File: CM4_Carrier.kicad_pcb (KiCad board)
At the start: 4 copper layers, 160 x 90 mm, 87 parts, among them J1 Conn_01x03, J10 690-019-298-412, J11 USB_OTG, J12 10018783-11200TLF, J13 BM04B-GHS-TBT(LF)(SN)(N), J14 BM04B-GHS-TBT(LF)(SN)(N), J15 Conn_01x22_Female, J17 Molex 470531000, J18 BM04B-GHS-TBT(LF)(SN)(N), J19 XT30, J2 Conn_02x07_Odd_Even, J20 AMP171826-4, J21 BM04B-GHS-TBT(LF)(SN)(N), J3 Conn_01x03, J4 Conn_01x22_Female, J5 Conn_01x22_Female, J7 Micro_SD_Card_Det, Q1 DMP3013SFV-7, U1 TPD4EUSB30, U11 EMC2301-1-ACZL-TR, U12 RT9742SNGV, U13 FSUSB42MUX, U18 RT9742GGJ5, U2 TPD4EUSB30, U3 MagJack-A70-112-331N126, U4 TPD4EUSB30, U5 74LVC1G07SE-7, U6 USB2514B-I/M2, U7 AP22653W6, U9 74LVC1G07SE-7, Y1 24MHz

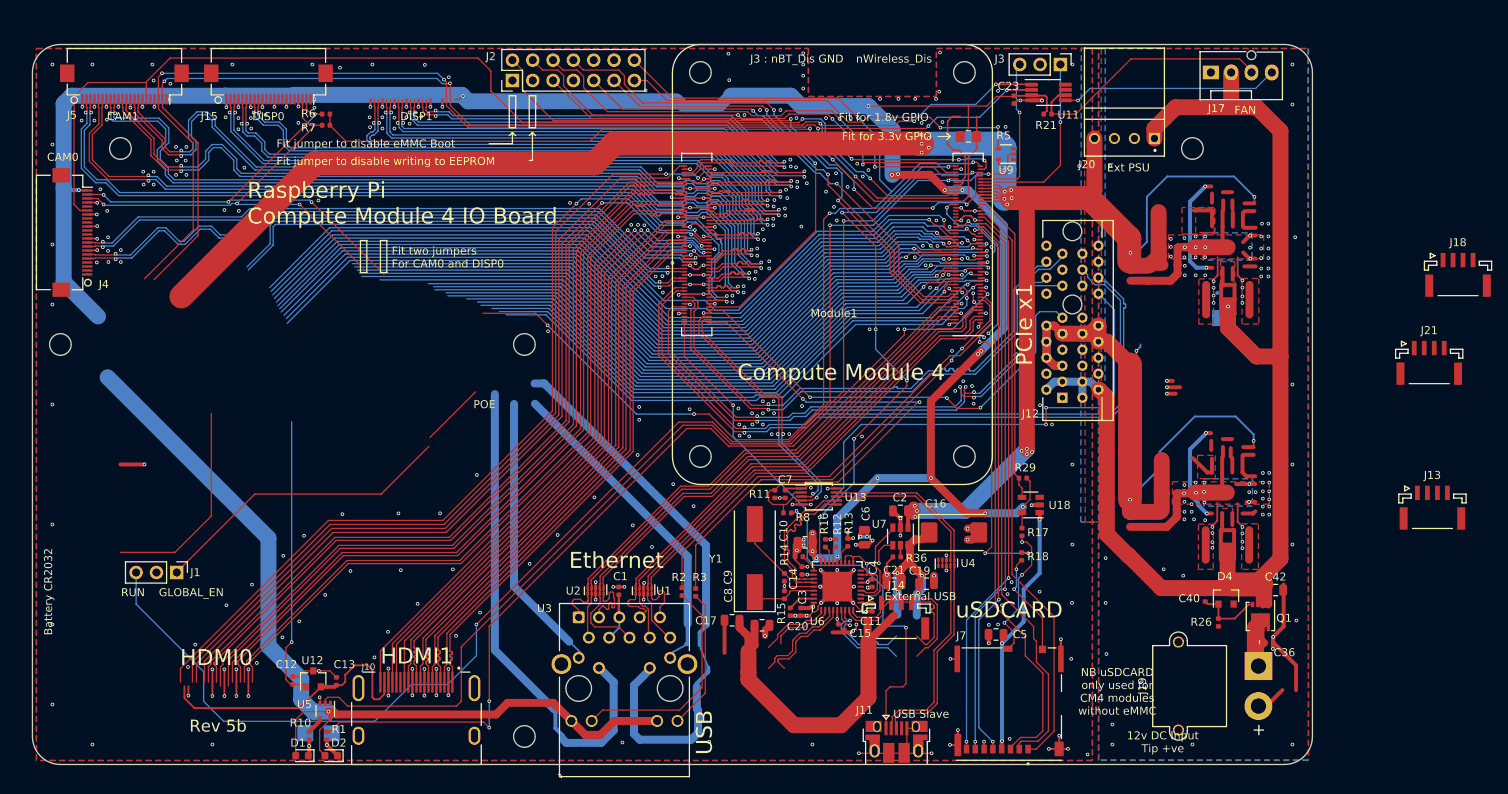
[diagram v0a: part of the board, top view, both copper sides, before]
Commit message: added original CM4IO pcb as starting point
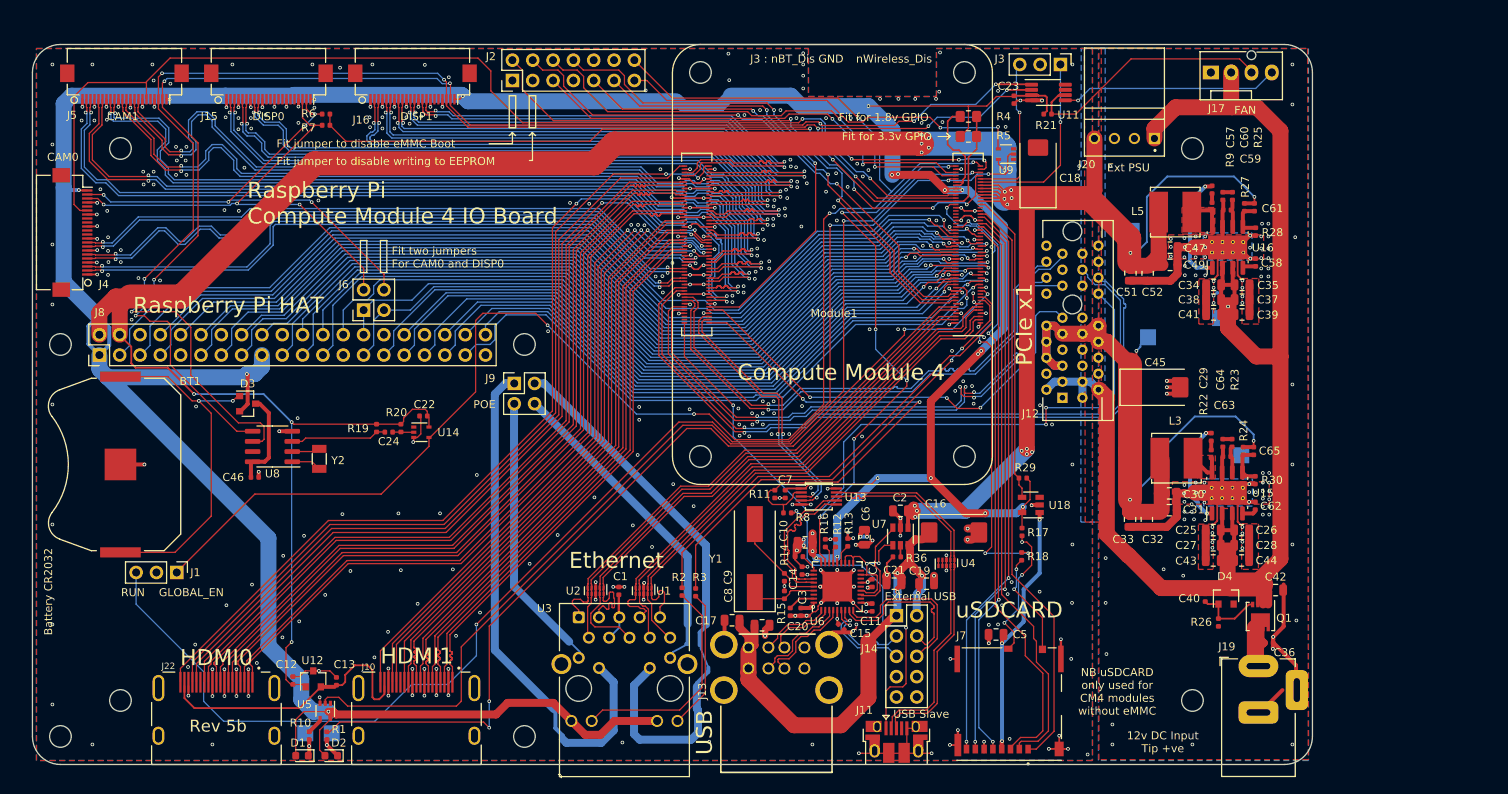
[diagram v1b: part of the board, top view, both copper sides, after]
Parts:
- removed J18, J21: BM04B-GHS-TBT(LF)(SN)(N), Connectors_JST:JST_GH_SM04B-GHS-TB_04x1.25mm_Angled
- added BT1: Battery_Cell, Battery:BatteryHolder_Keystone_3034_1x20mm, F.Cu at (90.0, 122.5)
- added C18: 100uF, Capacitor_Tantalum_SMD:CP_EIA-7343-31_Kemet-D, F.Cu at (204.7, 86.0)
- added C22: 100n, Capacitor_SMD:C_0402_1005Metric, F.Cu at (127.9, 116.4)
- added C24: 100n, Capacitor_SMD:C_0402_1005Metric, F.Cu at (123.5, 118.5)
- added C25: 10u 35v, Capacitor_SMD:C_0805_2012Metric, F.Cu at (226.6, 130.7)
- added C26: 10u 35v, Capacitor_SMD:C_0805_2012Metric, F.Cu at (230.2, 130.7)
- added C27: 10u 35v, Capacitor_SMD:C_0805_2012Metric, F.Cu at (226.6, 132.6)
- added C28: 10u 35v, Capacitor_SMD:C_0805_2012Metric, F.Cu at (230.2, 132.6)
- added C29: 100n, Capacitor_SMD:C_0402_1005Metric, F.Cu at (226.3, 119.1)
- added C30: 10u, Capacitor_SMD:C_0805_2012Metric, F.Cu at (221.1, 126.1)
- added C31: 10u, Capacitor_SMD:C_0805_2012Metric, F.Cu at (221.1, 128.2)
- added C32: 10u, Capacitor_SMD:C_0805_2012Metric, F.Cu at (218.3, 129.4)
- added C33: 10u, Capacitor_SMD:C_0805_2012Metric, F.Cu at (216.2, 129.4)
- added C34: 10u 35v, Capacitor_SMD:C_0805_2012Metric, F.Cu at (226.7, 100.0)
- added C35: 10u 35v, Capacitor_SMD:C_0805_2012Metric, F.Cu at (230.2, 100.0)
- added C37: 10u 35v, Capacitor_SMD:C_0805_2012Metric, F.Cu at (230.2, 101.9)
- added C38: 10u 35v, Capacitor_SMD:C_0805_2012Metric, F.Cu at (226.7, 101.9)
- added C39: 10u 35v, Capacitor_SMD:C_0805_2012Metric, F.Cu at (230.2, 103.8)
- added C41: 10u 35v, Capacitor_SMD:C_0805_2012Metric, F.Cu at (226.7, 103.8)
- added C43: 10u 35v, Capacitor_SMD:C_0805_2012Metric, F.Cu at (226.6, 134.5)
- added C44: 10u 35v, Capacitor_SMD:C_0805_2012Metric, F.Cu at (230.2, 134.5)
- added C45: 100uF, Capacitor_Tantalum_SMD:CP_EIA-7343-31_Kemet-D, F.Cu at (219.3, 112.8)
- added C46: 100n, Capacitor_SMD:C_0402_1005Metric, F.Cu at (106.8, 124.1)
- added C47: 10u, Capacitor_SMD:C_0805_2012Metric, F.Cu at (221.2, 95.4)
- added C49: 10u, Capacitor_SMD:C_0805_2012Metric, F.Cu at (221.2, 97.5)
- added C51: 10u, Capacitor_SMD:C_0805_2012Metric, F.Cu at (216.2, 98.6)
- added C52: 10u, Capacitor_SMD:C_0805_2012Metric, F.Cu at (218.4, 98.6)
- added C57: 100n, Capacitor_SMD:C_0402_1005Metric, F.Cu at (226.4, 88.2)
- added C58: 100n, Capacitor_SMD:C_0402_1005Metric, F.Cu at (231.9, 97.2)
- added C59: nf, Capacitor_SMD:C_0402_1005Metric, F.Cu at (228.3, 90.7)
- added C60: 1.2nF, Capacitor_SMD:C_0402_1005Metric, F.Cu at (227.8, 89.0)
- added C61: nf, Capacitor_SMD:C_0402_1005Metric, F.Cu at (231.8, 90.3)
- added C62: 100n, Capacitor_SMD:C_0402_1005Metric, F.Cu at (231.8, 127.7)
- added C63: nf, Capacitor_SMD:C_0402_1005Metric, F.Cu at (228.3, 121.5)
- added C64: 1.2nF, Capacitor_SMD:C_0402_1005Metric, F.Cu at (227.8, 119.8)
- added C65: nf, Capacitor_SMD:C_0402_1005Metric, F.Cu at (231.7, 120.8)
- added D3: BAT54C-7-F, Package_TO_SOT_SMD:SOT-23, F.Cu at (105.9, 114.9)
- added H1: MountingHole, MountingHole:MountingHole_2.7mm_M2.5, F.Cu at (90.0, 152.0)
- added H2: MountingHole, MountingHole:MountingHole_2.7mm_M2.5, F.Cu at (82.5, 156.5)
- added H8: MountingHole, MountingHole:MountingHole_2.7mm_M2.5, F.Cu at (224.0, 152.0)
- added J16: Conn_01x22_Female, CM4IO:Hirose_FH12-22S-0.5SH_1x22-1MP_P0.50mm_Horizontal, F.Cu at (126.5, 75.0)
- added J22: 690-019-298-412, CM4IO:EDAC 690-019-298-412, F.Cu at (102.0, 150.4)
- added J6: THD-02-R, Connector_PinHeader_2.54mm:PinHeader_2x02_P2.54mm_Vertical, F.Cu at (120.4, 103.2)
- added J8: THD-20-R, Connector_PinHeader_2.54mm:PinHeader_2x20_P2.54mm_Vertical, F.Cu at (87.4, 108.8)
- added J9: THD-02-R, Connector_PinHeader_2.54mm:PinHeader_2x02_P2.54mm_Vertical, F.Cu at (139.2, 112.4)
- added L3: SRN6045TA-3R3Y, Inductor_SMD:L_Bourns_SRN6045TA, F.Cu at (222.0, 121.7)
- added L5: SRN6045TA-3R3Y, Inductor_SMD:L_Bourns_SRN6045TA, F.Cu at (221.8, 91.0)
- added R19: 510K 1%, Resistor_SMD:R_0402_1005Metric, F.Cu at (122.0, 117.9)
- added R20: 510K 1%, Resistor_SMD:R_0402_1005Metric, F.Cu at (125.1, 117.9)
- added R22: 10R, Resistor_SMD:R_0402_1005Metric, F.Cu at (226.3, 121.2)
- added R23: 12K 1%, Resistor_SMD:R_0402_1005Metric, F.Cu at (228.9, 119.8)
- added R24: 47K 1%, Resistor_SMD:R_0402_1005Metric, F.Cu at (230.3, 120.8)
- added R25: 20K 1%, Resistor_SMD:R_0402_1005Metric, F.Cu at (229.0, 89.0)
- added R27: 12K 1%, Resistor_SMD:R_0402_1005Metric, F.Cu at (230.5, 90.3)
- added R28: 2.2K 1%, Resistor_SMD:R_0402_1005Metric, F.Cu at (231.9, 93.4)
- added R30: 15K 1%, Resistor_SMD:R_0402_1005Metric, F.Cu at (231.8, 124.5)
- added R4: nf, Resistor_SMD:R_0805_2012Metric_Pad1.15x1.40mm_HandSolder, F.Cu at (196.0, 79.0)
- added R9: 10R, Resistor_SMD:R_0402_1005Metric, F.Cu at (226.4, 90.2)
- added TP1: TestPoint, TestPoint:TestPoint_Pad_2.0x2.0mm, B.Cu at (218.4, 106.6)
- added TP4: TestPoint, TestPoint:TestPoint_Pad_2.0x2.0mm, B.Cu at (216.4, 93.3)
- added TP6: TestPoint, TestPoint:TestPoint_Pad_2.0x2.0mm, B.Cu at (230.1, 121.3)
- added U14: 74LVC1G07SE-7, Package_TO_SOT_SMD:SOT-353_SC-70-5, F.Cu at (127.6, 118.5)
- added U15: AP64501SP-13, CM4IO:SOIC-8-1EP_3.9x4.9mm_P1.27mm_EP2.95x4.9mm_Mask2.71x3.4mm_ThermalVias, F.Cu at (228.3, 126.1)
- added U16: AP64501SP-13, Package_SO:SOIC-8-1EP_3.9x4.9mm_P1.27mm_EP2.95x4.9mm_Mask2.71x3.4mm_ThermalVias, F.Cu at (228.4, 95.3)
- added U8: PCF85063AT/AAZ, Package_SO:SOIC-8_3.9x4.9mm_P1.27mm, F.Cu at (109.0, 120.2)
- added Y2: X32K768S301, Crystal:Crystal_SMD_3215-2Pin_3.2x1.5mm, F.Cu at (114.8, 121.8)
- J13: value BM04B-GHS-TBT(LF)(SN)(N) -> 690-008-221-904; footprint Connectors_JST:JST_GH_SM04B-GHS-TB_04x1.25mm_Angled -> CM4IO:MOLEX_USB_67298-4090
- J14: value BM04B-GHS-TBT(LF)(SN)(N) -> Conn_02x05_Odd_Even; footprint Connectors_JST:JST_GH_SM04B-GHS-TB_04x1.25mm_Angled -> Connector_PinHeader_2.54mm:PinHeader_2x05_P2.54mm_Vertical
- J19: value XT30 -> Barrel_Jack; footprint XT-30:AMASS_XT30PW-M_1x02_P2.50mm_Horizontal -> CM4IO:BarrelJack_Horizontal
- moved J13 85.2 mm to (172.0, 150.7)
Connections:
- C16 pad 1: /USB2-HUB/VBUS_HP -> /USB2-HUB/VBUS
- C17 pad 1: /USB2-HUB/VBUS_HP -> /USB2-HUB/VBUS
- C19 pad 1: /USB2-HUB/VBUS_HP -> /USB2-HUB/VBUS
- C20 pad 1: /USB2-HUB/VBUS_HP -> /USB2-HUB/VBUS
- C21 pad 1: /USB2-HUB/VBUS_HP -> /USB2-HUB/VBUS
- C40 pad 1: /PSUs/+12v -> /+12v
- C42 pad 1: /PSUs/+12v -> /+12v
- D4 pad 1: /PSUs/+12v -> /+12v
- J12 pad A2: /PCIe-connector/+12v -> /+12v
- J12 pad A3: /PCIe-connector/+12v -> /+12v
- J12 pad B1: /PCIe-connector/+12v -> /+12v
- J12 pad B2: /PCIe-connector/+12v -> /+12v
- J12 pad B3: /PCIe-connector/+12v -> /+12v
- J13 pad 1: /USB2-HUB/VBUS_HP -> /USB2-HUB/VBUS
- J13 pad 2: /USB2-HUB/HD2_N -> /USB2-HUB/HD1_N
- J13 pad 3: /USB2-HUB/HD2_P -> /USB2-HUB/HD1_P
- J14 pad 1: /USB2-HUB/VBUS_HP -> /USB2-HUB/VBUS
- J14 pad 2: /USB2-HUB/HD1_N -> /USB2-HUB/VBUS
- J14 pad 3: /USB2-HUB/HD1_P -> /USB2-HUB/HD3_N
- J14 pad 4: GND -> /USB2-HUB/HD4_N
- J17 pad 2: /+5v -> /+12v
- J19 pad 1: GND -> Net-(C36-Pad1)
- J19 pad 2: Net-(C36-Pad1) -> GND
- J20 pad 1: (no net) -> /+12v
- Module1 pad 51: /CM4_GPIO ( Ethernet, GPIO, SDCARD)/UART0_RX -> /CM4_GPIO ( Ethernet, GPIO, SDCARD)/GPIO15
- Module1 pad 55: /CM4_GPIO ( Ethernet, GPIO, SDCARD)/UART0_TX -> /CM4_GPIO ( Ethernet, GPIO, SDCARD)/GPIO14
- Q1 pad 1: /PSUs/+12v -> /+12v
- Q1 pad 2: /PSUs/+12v -> /+12v
- Q1 pad 3: /PSUs/+12v -> /+12v
- TP2 pad 1: /PSUs/+12v -> /+12v
- U11 pad 1: /FAN/SDA -> /SDA0
- U11 pad 2: /FAN/SCL -> /SCL0
- U6 pad 19: /USB2-HUB/nOCS2 -> /USB2-HUB/nOCS1
- U6 pad 21: /USB2-HUB/nOCS2 -> /USB2-HUB/nOCS1
- U7 pad 6: /USB2-HUB/VBUS_HP -> /USB2-HUB/VBUS
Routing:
- net GND: track 361.1 -> 882.7 mm, vias 477 -> 487
- net 12: track 189.7 -> 0.00 mm
- net /+12v: track 0.00 -> 189.7 mm, vias 0 -> 1
- net /CM4_GPIO ( Ethernet, GPIO, SDCARD)/GPIO14: track 0.00 -> 117.8 mm, vias 0 -> 1
- net /CM4_GPIO ( Ethernet, GPIO, SDCARD)/GPIO15: track 0.00 -> 114.7 mm, vias 0 -> 1
- net /CM4_GPIO ( Ethernet, GPIO, SDCARD)/UART0_TX: track 101.6 -> 0.00 mm, vias 1 -> 0
- net /CM4_GPIO ( Ethernet, GPIO, SDCARD)/UART0_RX: track 101.0 -> 0.00 mm, vias 1 -> 0
- net /USB2-HUB/VBUS: track 0.00 -> 69.2 mm, vias 0 -> 4
- net /+5v: track 301.3 -> 367.6 mm, vias 21 -> 23
- net /USB2-HUB/VBUS_HP: track 53.4 -> 0.00 mm, vias 4 -> 0
- net Net-(BT1-Pad1): track 0.00 -> 44.4 mm, vias 0 -> 2
- net 203: track 41.8 -> 0.00 mm
- net /+3.3v: track 419.7 -> 461.1 mm, vias 27 -> 28
- net /SCL0: track 167.3 -> 201.4 mm, vias 6 -> 8
- net /SDA0: track 165.6 -> 194.6 mm, vias 6 -> 8
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- added copper zone on F.Cu, net /+12v
- removed copper zone on F.Cu, net /PSUs/+12v
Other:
- board text added: "Raspberry Pi HAT"

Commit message: library management
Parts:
- removed BT1: Battery_Cell, Battery:BatteryHolder_Keystone_3034_1x20mm
- removed C32, C33, C47, C49, C51, C52: 10u, Capacitor_SMD:C_0805_2012Metric
- removed C34, C35, C37, C38, C39, C41, C43, C44: 10u 35v, Capacitor_SMD:C_0805_2012Metric
- removed C45: 100uF, Capacitor_Tantalum_SMD:CP_EIA-7343-31_Kemet-D
- removed C46, C57, C58, C62: 100n, Capacitor_SMD:C_0402_1005Metric
- removed C59, C61, C63, C65: nf, Capacitor_SMD:C_0402_1005Metric
- removed C60, C64: 1.2nF, Capacitor_SMD:C_0402_1005Metric
- removed D3: BAT54C-7-F, Package_TO_SOT_SMD:SOT-23
- removed J16: Conn_01x22_Female, CM4IO:Hirose_FH12-22S-0.5SH_1x22-1MP_P0.50mm_Horizontal
- removed J19: Barrel_Jack, CM4IO:BarrelJack_Horizontal
- removed J22: 690-019-298-412, CM4IO:EDAC 690-019-298-412
- removed L3, L5: SRN6045TA-3R3Y, Inductor_SMD:L_Bourns_SRN6045TA
- removed R20: 510K 1%, Resistor_SMD:R_0402_1005Metric
- removed R22: 10R, Resistor_SMD:R_0402_1005Metric
- removed R23, R27: 12K 1%, Resistor_SMD:R_0402_1005Metric
- removed R24: 47K 1%, Resistor_SMD:R_0402_1005Metric
- removed R25: 20K 1%, Resistor_SMD:R_0402_1005Metric
- removed R28: 2.2K 1%, Resistor_SMD:R_0402_1005Metric
- removed R30: 15K 1%, Resistor_SMD:R_0402_1005Metric
- removed TP1, TP2, TP4, TP6: TestPoint, TestPoint:TestPoint_Pad_2.0x2.0mm
- removed U14: 74LVC1G07SE-7, Package_TO_SOT_SMD:SOT-353_SC-70-5
- removed U15: AP64501SP-13, CM4IO:SOIC-8-1EP_3.9x4.9mm_P1.27mm_EP2.95x4.9mm_Mask2.71x3.4mm_ThermalVias
- removed U16: AP64501SP-13, Package_SO:SOIC-8-1EP_3.9x4.9mm_P1.27mm_EP2.95x4.9mm_Mask2.71x3.4mm_ThermalVias
- removed Y2: X32K768S301, Crystal:Crystal_SMD_3215-2Pin_3.2x1.5mm
- added C48: 10u, Capacitor_SMD:C_0805_2012Metric, F.Cu at (119.6, 101.0)
- added C50: 100uF, Capacitor_Tantalum_SMD:CP_EIA-7343-31_Kemet-D, F.Cu at (108.0, 102.4)
- added C53: 10u, Capacitor_SMD:C_0805_2012Metric, F.Cu at (115.2, 101.0)
- added C54: 10u, Capacitor_SMD:C_0805_2012Metric, F.Cu at (125.8, 90.2)
- added C55: 10u, Capacitor_SMD:C_0805_2012Metric, F.Cu at (115.2, 104.0)
- added C56: 10u, Capacitor_SMD:C_0805_2012Metric, F.Cu at (125.8, 93.2)
- added J18: BM04B-GHS-TBT(LF)(SN)(N), Connectors_JST:JST_GH_SM04B-GHS-TB_04x1.25mm_Angled, F.Cu at (151.2, 38.4)
- added J21: BM04B-GHS-TBT(LF)(SN)(N), Connectors_JST:JST_GH_SM04B-GHS-TB_04x1.25mm_Angled, F.Cu at (160.4, 38.4)
- added L1: 4.7uH, Open-HD:IND_XAL6060-472MEB, F.Cu at (139.4, 94.7)
- added R31: 49.9k, Resistor_SMD:R_0402_1005Metric, F.Cu at (130.2, 85.2)
- added U10: AP22653W6, Package_TO_SOT_SMD:SOT-23-6, F.Cu at (126.1, 86.4)
- C18: value 100uF -> 10uF; footprint Capacitor_Tantalum_SMD:CP_EIA-7343-31_Kemet-D -> Capacitor_SMD:C_1210_3225Metric
- C22: value 100n -> 10uF; footprint Capacitor_SMD:C_0402_1005Metric -> Capacitor_SMD:C_1210_3225Metric
- C24: value 100n -> 220nF; footprint Capacitor_SMD:C_0402_1005Metric -> Capacitor_SMD:C_0603_1608Metric
- C25: value 10u 35v -> 1uF; footprint Capacitor_SMD:C_0805_2012Metric -> Capacitor_SMD:C_0402_1005Metric
- C26: value 10u 35v -> 100nF; footprint Capacitor_SMD:C_0805_2012Metric -> Capacitor_SMD:C_0402_1005Metric
- C27: value 10u 35v -> 10pF; footprint Capacitor_SMD:C_0805_2012Metric -> Capacitor_SMD:C_0402_1005Metric
- C28: value 10u 35v -> 22uF
- C29: value 100n -> 22uF; footprint Capacitor_SMD:C_0402_1005Metric -> Capacitor_SMD:C_0805_2012Metric
- C30: value 10u -> 22uF
- C31: value 10u -> 100nF; footprint Capacitor_SMD:C_0805_2012Metric -> Capacitor_SMD:C_0603_1608Metric
- J13: value 690-008-221-904 -> BM04B-GHS-TBT(LF)(SN)(N); footprint CM4IO:MOLEX_USB_67298-4090 -> Connectors_JST:JST_GH_SM04B-GHS-TB_04x1.25mm_Angled
- J14: value Conn_02x05_Odd_Even -> BM04B-GHS-TBT(LF)(SN)(N); footprint Connector_PinHeader_2.54mm:PinHeader_2x05_P2.54mm_Vertical -> Connectors_JST:JST_GH_SM04B-GHS-TB_04x1.25mm_Angled
- J15: footprint CM4IO:Hirose_FH12-22S-0.5SH_1x22-1MP_P0.50mm_Horizontal -> Connector_FFC-FPC:Hirose_FH12-22S-0.5SH_1x22-1MP_P0.50mm_Horizontal
- J4, J5: value Conn_01x22_Female -> DF40C-24DP-0.4V_51_; footprint CM4IO:Hirose_FH12-22S-0.5SH_1x22-1MP_P0.50mm_Horizontal -> Open-HD:DF40C24DP04V51
- J8: value THD-20-R -> HDMI_D_1.4; footprint Connector_PinHeader_2.54mm:PinHeader_2x20_P2.54mm_Vertical -> Connector_HDMI:HDMI_Micro-D_Molex_46765-0x01
- J9: value THD-02-R -> Conn_02x08_Odd_Even; footprint Connector_PinHeader_2.54mm:PinHeader_2x02_P2.54mm_Vertical -> Connector_PinHeader_2.54mm:PinHeader_2x08_P2.54mm_Vertical
- R19: value 510K 1% -> 24.9k
- R4: value nf -> 100k; footprint Resistor_SMD:R_0805_2012Metric_Pad1.15x1.40mm_HandSolder -> Resistor_SMD:R_0402_1005Metric
- R9: value 10R -> 100k
- U11: footprint Package_SO:MSOP-8_3x3mm_P0.65mm -> Package_SO:SOIC-8_5.23x5.23mm_P1.27mm
- U8: value PCF85063AT/AAZ -> LMR33640DDDAR; footprint Package_SO:SOIC-8_3.9x4.9mm_P1.27mm -> Open-HD:NOPB
- moved J13 119.0 mm to (132.7, 38.4), turned to 180 degrees
- moved C1 113.7 mm to (259.4, 176.7)
- moved R2 113.7 mm to (267.2, 176.8)
- moved U3 113.7 mm to (260.1, 188.9)
- moved R3 113.7 mm to (268.9, 176.9)
- moved U1 113.7 mm to (262.4, 176.7)
- moved U2 113.7 mm to (256.4, 176.7)
- moved J14 112.4 mm to (141.9, 38.4), turned to 180 degrees
- moved J4 98.5 mm to (173.4, 52.2), turned to 90 degrees
- moved J5 96.5 mm to (184.3, 52.3), turned to 90 degrees
- moved C10 94.0 mm to (148.8, 222.4)
- moved C14 94.0 mm to (148.4, 225.9)
- moved C16 94.0 mm to (167.4, 221.1)
- moved C17 94.0 mm to (139.7, 232.1)
- moved C19 94.0 mm to (164.0, 227.5)
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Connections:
- C16 pad 1: /USB2-HUB/VBUS -> /USB2-HUB/VBUS_HP
- C17 pad 1: /USB2-HUB/VBUS -> /USB2-HUB/VBUS_HP
- C18 pad 1: /+5v -> /PSUs/+12v
- C19 pad 1: /USB2-HUB/VBUS -> /USB2-HUB/VBUS_HP
- C20 pad 1: /USB2-HUB/VBUS -> /USB2-HUB/VBUS_HP
- C21 pad 1: /USB2-HUB/VBUS -> /USB2-HUB/VBUS_HP
- C22 pad 1: /+5v -> /PSUs/+12v
- C24 pad 1: Net-(C24-Pad1) -> /PSUs/+12v
- C24 pad 2: /RTC , Wakeup, FAN/nRTC_INT -> GND
- C25 pad 1: /+12v -> Net-(C25-Pad1)
- C26 pad 1: /+12v -> Net-(C26-Pad1)
- C26 pad 2: GND -> Net-(C26-Pad2)
- C27 pad 1: /+12v -> /+5v
- C27 pad 2: GND -> Net-(C27-Pad2)
- C28 pad 1: /+12v -> /+5v
- C29 pad 1: Net-(C29-Pad1) -> /+5v
- C29 pad 2: Net-(C29-Pad2) -> GND
- C30 pad 1: /PCIe-connector/+3.3v -> /+5v
- C31 pad 1: /PCIe-connector/+3.3v -> /+5v
- C40 pad 1: /+12v -> /PSUs/+12v
- C42 pad 1: /+12v -> /PSUs/+12v
- D4 pad 1: /+12v -> /PSUs/+12v
- J12 pad A2: /+12v -> Net-(J12-PadA2)
- J12 pad A3: /+12v -> Net-(J12-PadA2)
- J12 pad B1: /+12v -> Net-(J12-PadB1)
- J12 pad B2: /+12v -> Net-(J12-PadB1)
- J12 pad B3: /+12v -> Net-(J12-PadB1)
- J13 pad 1: /USB2-HUB/VBUS -> /USB2-HUB/VBUS_HP
- J13 pad 2: /USB2-HUB/HD1_N -> /USB2-HUB/HD2_N
- J13 pad 3: /USB2-HUB/HD1_P -> /USB2-HUB/HD2_P
- J14 pad 1: /USB2-HUB/VBUS -> /USB2-HUB/VBUS_HP
- J14 pad 2: /USB2-HUB/VBUS -> /USB2-HUB/HD1_N
- J14 pad 3: /USB2-HUB/HD3_N -> /USB2-HUB/HD1_P
- J14 pad 4: /USB2-HUB/HD4_N -> GND
- J17 pad 2: /+12v -> /+5v
- J4 pad 1: GND -> /CM4_HighSpeed/CAM1_D0_N
- J4 pad 10: GND -> Net-(J4-Pad10)
- J4 pad 11: Net-(J4-Pad11) -> GND
- J4 pad 13: GND -> /CM4_HighSpeed/CAM1_C_N
- J4 pad 14: Net-(J4-Pad14) -> /CAM_GPIO
- J4 pad 15: Net-(J4-Pad15) -> /CM4_HighSpeed/CAM1_C_P
- J4 pad 16: GND -> Net-(J4-Pad16)
- J4 pad 17: /CAM_GPIO -> GND
- J4 pad 18: Net-(J4-Pad18) -> GND
- J4 pad 19: GND -> /CM4_HighSpeed/CAM1_D2_N
- J4 pad 2: /CM4_HighSpeed/CAM0_D0_N -> /CM4_HighSpeed/CAM1_D3_N
- J4 pad 20: /CM4_HighSpeed/SCL1 -> /SCL0
- J4 pad 21: /CM4_HighSpeed/SDA1 -> /CM4_HighSpeed/CAM1_D2_P
- J4 pad 22: /+3.3v -> /SDA0
- J4 pad 3: /CM4_HighSpeed/CAM0_D0_P -> /CM4_HighSpeed/CAM1_D0_P
- J4 pad 4: GND -> /CM4_HighSpeed/CAM1_D3_P
- J4 pad 5: /CM4_HighSpeed/CAM0_D1_N -> GND
- J4 pad 6: /CM4_HighSpeed/CAM0_D1_P -> GND
- J4 pad 7: GND -> /CM4_HighSpeed/CAM1_D1_N
- J4 pad 8: /CM4_HighSpeed/CAM0_C_N -> Net-(J4-Pad8)
- J4 pad 9: /CM4_HighSpeed/CAM0_C_P -> /CM4_HighSpeed/CAM1_D1_P
- J5 pad 10: GND -> Net-(J5-Pad10)
- J5 pad 11: /CM4_HighSpeed/CAM1_D2_N -> /CM4_HighSpeed/CAM0_D1_P
- J5 pad 12: /CM4_HighSpeed/CAM1_D2_P -> GND
- J5 pad 14: /CM4_HighSpeed/CAM1_D3_N -> /CAM_GPIO
- J5 pad 15: /CM4_HighSpeed/CAM1_D3_P -> /CM4_HighSpeed/CAM0_C_N
- J5 pad 16: GND -> Net-(J5-Pad16)
- J5 pad 17: /CAM_GPIO -> /CM4_HighSpeed/CAM0_C_P
- J5 pad 18: Net-(J5-Pad18) -> GND
- J5 pad 2: /CM4_HighSpeed/CAM1_D0_N -> Net-(J5-Pad2)
- J5 pad 20: /SCL0 -> /CM4_HighSpeed/SCL1
- J5 pad 21: /SDA0 -> Net-(J5-Pad21)
- J5 pad 22: /+3.3v -> /CM4_HighSpeed/SDA1
- J5 pad 3: /CM4_HighSpeed/CAM1_D0_P -> /CM4_HighSpeed/CAM0_D0_N
- J5 pad 4: GND -> Net-(J5-Pad4)
- J5 pad 5: /CM4_HighSpeed/CAM1_D1_N -> /CM4_HighSpeed/CAM0_D0_P
- J5 pad 6: /CM4_HighSpeed/CAM1_D1_P -> Net-(J5-Pad6)
- J5 pad 8: /CM4_HighSpeed/CAM1_C_N -> Net-(J5-Pad8)
- J5 pad 9: /CM4_HighSpeed/CAM1_C_P -> /CM4_HighSpeed/CAM0_D1_N
- J8 pad 1: /+3.3v -> /CM4_HighSpeed/HDMI0_HOTPLUG
- J8 pad 10: /CM4_GPIO ( Ethernet, GPIO, SDCARD)/GPIO15 -> GND
- J8 pad 11: /CM4_GPIO ( Ethernet, GPIO, SDCARD)/GPIO17 -> /CM4_HighSpeed/HDMI0_D0_N
- J8 pad 12: /CM4_GPIO ( Ethernet, GPIO, SDCARD)/GPIO18 -> /CM4_HighSpeed/HDMI0_CK_P
- J8 pad 13: /CM4_GPIO ( Ethernet, GPIO, SDCARD)/GPIO27 -> GND
- J8 pad 14: GND -> /CM4_HighSpeed/HDMI0_CK_N
- J8 pad 15: /CM4_GPIO ( Ethernet, GPIO, SDCARD)/GPIO22 -> /CM4_HighSpeed/HDMI0_CEC
- J8 pad 16: /CM4_GPIO ( Ethernet, GPIO, SDCARD)/GPIO23 -> GND
- J8 pad 17: /+3.3v -> /CM4_HighSpeed/HDMI0_SCL
- J8 pad 18: /CM4_GPIO ( Ethernet, GPIO, SDCARD)/GPIO24 -> /CM4_HighSpeed/HDMI0_SDA
- J8 pad 19: /CM4_GPIO ( Ethernet, GPIO, SDCARD)/GPIO10 -> /CM4_HighSpeed/HDMI_5v
- J8 pad 2: /+5v -> Net-(J8-Pad2)
- J8 pad 3: /CM4_GPIO ( Ethernet, GPIO, SDCARD)/GPIO2 -> /CM4_HighSpeed/HDMI0_D2_P
- J8 pad 4: /+5v -> GND
- J8 pad 5: /CM4_GPIO ( Ethernet, GPIO, SDCARD)/GPIO3 -> /CM4_HighSpeed/HDMI0_D2_N
- J8 pad 6: GND -> /CM4_HighSpeed/HDMI0_D1_P
- J8 pad 7: /CM4_GPIO ( Ethernet, GPIO, SDCARD)/GPIO4 -> GND
- J8 pad 8: /CM4_GPIO ( Ethernet, GPIO, SDCARD)/GPIO14 -> /CM4_HighSpeed/HDMI0_D1_N
- J8 pad 9: GND -> /CM4_HighSpeed/HDMI0_D0_P
- J9 pad 1: /CM4_GPIO ( Ethernet, GPIO, SDCARD)/TR1_TAP -> /CM4_GPIO ( Ethernet, GPIO, SDCARD)/GPIO10
- J9 pad 2: /CM4_GPIO ( Ethernet, GPIO, SDCARD)/TR2_TAP -> GND
- J9 pad 3: /CM4_GPIO ( Ethernet, GPIO, SDCARD)/TR0_TAP -> /CM4_GPIO ( Ethernet, GPIO, SDCARD)/GPIO22
- J9 pad 4: /CM4_GPIO ( Ethernet, GPIO, SDCARD)/TR3_TAP -> GND
- Module1 pad 51: /CM4_GPIO ( Ethernet, GPIO, SDCARD)/GPIO15 -> /CM4_GPIO ( Ethernet, GPIO, SDCARD)/UART0_RX
- Module1 pad 55: /CM4_GPIO ( Ethernet, GPIO, SDCARD)/GPIO14 -> /CM4_GPIO ( Ethernet, GPIO, SDCARD)/UART0_TX
- Q1 pad 1: /+12v -> /PSUs/+12v
- Q1 pad 2: /+12v -> /PSUs/+12v
- Q1 pad 3: /+12v -> /PSUs/+12v
- R19 pad 1: /RTC , Wakeup, FAN/nRTC_INT -> Net-(C27-Pad2)
- R19 pad 2: /+5v -> GND
- R4 pad 1: /CM4_GPIO ( Ethernet, GPIO, SDCARD)/+1.8v -> Net-(R4-Pad1)
- R4 pad 2: /GPIO_VREF -> /+5v
- R9 pad 1: Net-(L5-Pad1) -> /+5v
- R9 pad 2: Net-(C57-Pad1) -> Net-(C27-Pad2)
- U11 pad 1: /SDA0 -> /FAN/SDA
- U11 pad 2: /SCL0 -> /FAN/SCL
- U6 pad 19: /USB2-HUB/nOCS1 -> /USB2-HUB/nOCS2
- U6 pad 21: /USB2-HUB/nOCS1 -> /USB2-HUB/nOCS2
- U7 pad 6: /USB2-HUB/VBUS -> /USB2-HUB/VBUS_HP
- U8 pad 1: Net-(U8-Pad1) -> GND
- U8 pad 2: Net-(U8-Pad2) -> /PSUs/+12v
- U8 pad 3: /RTC , Wakeup, FAN/nRTC_INT -> /PSUs/+12v
- U8 pad 4: GND -> Net-(R4-Pad1)
- U8 pad 5: /SDA0 -> Net-(C27-Pad2)
- U8 pad 6: /SCL0 -> Net-(C25-Pad1)
- U8 pad 7: Net-(U8-Pad7) -> Net-(C26-Pad1)
- U8 pad 8: Net-(C46-Pad1) -> Net-(C26-Pad2)
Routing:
- net GND: track 882.7 -> 0.00 mm, vias 487 -> 0
- net /+3.3v: track 461.1 -> 0.00 mm, vias 28 -> 0
- net /+5v: track 367.6 -> 0.00 mm, vias 23 -> 0
- net /SCL0: track 201.4 -> 0.00 mm, vias 8 -> 0
- net /GLOBAL_EN: track 196.2 -> 0.00 mm, vias 5 -> 0
- net /SDA0: track 194.6 -> 0.00 mm, vias 8 -> 0
- net /+12v: track 189.7 -> 0.00 mm, vias 1 -> 0
- net /CM4_GPIO ( Ethernet, GPIO, SDCARD)/RUN_PG: track 170.6 -> 0.00 mm, vias 4 -> 0
- net /CAM_GPIO: track 143.1 -> 0.00 mm, vias 4 -> 0
- net /CM4_GPIO ( Ethernet, GPIO, SDCARD)/nPWR_LED: track 128.9 -> 0.00 mm, vias 2 -> 0
- net /CM4_GPIO ( Ethernet, GPIO, SDCARD)/GPIO2: track 122.9 -> 0.00 mm, vias 1 -> 0
- net /CM4_GPIO ( Ethernet, GPIO, SDCARD)/GPIO3: track 119.8 -> 0.00 mm, vias 1 -> 0
- net /CM4_GPIO ( Ethernet, GPIO, SDCARD)/GPIO14: track 117.8 -> 0.00 mm, vias 1 -> 0
- net Net-(Module1-Pad21): track 116.6 -> 0.00 mm, vias 4 -> 0
- net /CM4_GPIO ( Ethernet, GPIO, SDCARD)/GPIO4: track 116.5 -> 0.00 mm, vias 1 -> 0
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- removed copper zone on F.Cu, net /+12v
- removed copper zone on B.Cu, net GND
- removed copper zone on F.Cu, net GND
- removed copper zone on In1.Cu, net GND
- removed copper zone on In2.Cu, net GND
- removed copper zone on F.Cu, net Net-(L3-Pad1)
- removed copper zone on F.Cu, net Net-(L5-Pad1)

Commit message: added 3D models
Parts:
- removed C42: 10u 35v, Capacitor_SMD:C_0805_2012Metric
- removed J20: AMP171826-4, 171826-4:TE_171826-4
- removed U3: MagJack-A70-112-331N126, CM4IO:TRJG0926HENL
- added J19: XT30, Open-HD:AMASS_XT30PW-M_1x02_P2.50mm_Horizontal, F.Cu at (143.7, 55.1)
- C1, C10, C11, C14, C15, C16, C17, C19, C2, C20, C21, C3, C4, C5, C6, C7, C8, C9, J15, R11, R12, R13, R14, R15, R16, R2, R3, R36, R8, U1, U13, U2, U4, U6, U7, Y1: moved to B.Cu
- J10: value 690-019-298-412 -> Conn_01x20; footprint CM4IO:EDAC 690-019-298-412 -> Connector_FFC-FPC:Molex_200528-0200_1x20-1MP_P1.00mm_Horizontal; moved to B.Cu
- J17: footprint Connector:FanPinHeader_1x04_P2.54mm_Vertical -> Open-HD:fan
- moved H7 262.1 mm to (344.4, 146.2)
- moved H2 255.5 mm to (337.4, 139.2)
- moved H3 251.0 mm to (330.5, 146.2)
- moved H1 247.5 mm to (337.4, 146.2)
- moved C12 211.5 mm to (-99.5, 162.5)
- moved C13 211.5 mm to (-94.1, 162.6)
- moved D1 211.5 mm to (-98.4, 171.9)
- moved D2 211.5 mm to (-94.7, 171.9)
- moved R1 211.5 mm to (-95.3, 169.4)
- moved R10 211.5 mm to (-97.5, 169.4)
- moved TP3 211.5 mm to (-94.7, 169.1)
- moved TP5 211.5 mm to (-98.0, 169.1)
- moved U12 211.5 mm to (-97.0, 162.3)
- moved U5 211.5 mm to (-95.5, 166.3)
- moved H4 190.8 mm to (330.5, 139.2)
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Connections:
- J10 pad 1: /CM4_HighSpeed/HDMI1_D2_P -> /CM4_GPIO ( Ethernet, GPIO, SDCARD)/TRD0_P
- J10 pad 10: /CM4_HighSpeed/HDMI1_CK_P -> /CM4_GPIO ( Ethernet, GPIO, SDCARD)/TRD3_N
- J10 pad 11: GND -> /CM4_GPIO ( Ethernet, GPIO, SDCARD)/TR0_TAP
- J10 pad 12: /CM4_HighSpeed/HDMI1_CK_N -> /CM4_GPIO ( Ethernet, GPIO, SDCARD)/TR1_TAP
- J10 pad 13: /CM4_HighSpeed/HDMI1_CEC -> /CM4_GPIO ( Ethernet, GPIO, SDCARD)/TR2_TAP
- J10 pad 14: Net-(J10-Pad14) -> /CM4_GPIO ( Ethernet, GPIO, SDCARD)/TR3_TAP
- J10 pad 15: /CM4_HighSpeed/HDMI1_SCL -> /+3.3v
- J10 pad 16: /CM4_HighSpeed/HDMI1_SDA -> Net-(J10-Pad16)
- J10 pad 17: GND -> /+3.3v
- J10 pad 18: /CM4_HighSpeed/HDMI_5v -> Net-(J10-Pad18)
- J10 pad 19: /CM4_HighSpeed/HDMI1_HOTPLUG -> Net-(J10-Pad19)
- J10 pad 2: GND -> /CM4_GPIO ( Ethernet, GPIO, SDCARD)/TRD0_N
- J10 pad 3: /CM4_HighSpeed/HDMI1_D2_N -> /CM4_GPIO ( Ethernet, GPIO, SDCARD)/TRD1_P
- J10 pad 4: /CM4_HighSpeed/HDMI1_D1_P -> /CM4_GPIO ( Ethernet, GPIO, SDCARD)/TRD1_N
- J10 pad 5: GND -> Net-(C1-Pad1)
- J10 pad 6: /CM4_HighSpeed/HDMI1_D1_N -> Net-(C1-Pad1)
- J10 pad 7: /CM4_HighSpeed/HDMI1_D0_P -> /CM4_GPIO ( Ethernet, GPIO, SDCARD)/TRD2_P
- J10 pad 8: GND -> /CM4_GPIO ( Ethernet, GPIO, SDCARD)/TRD2_N
- J10 pad 9: /CM4_HighSpeed/HDMI1_D0_N -> /CM4_GPIO ( Ethernet, GPIO, SDCARD)/TRD3_P
- R2 pad 1: Net-(R2-Pad1) -> Net-(J10-Pad16)
- R3 pad 1: Net-(R3-Pad1) -> Net-(J10-Pad18)
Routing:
- added copper zone on In1.Cu, net /+3.3v
- removed copper zone on In2.Cu, net /+3.3v
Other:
- board outline removed
- board text removed: "Battery CR2032"
- board text removed: "CAM0"
- board text removed: "CAM1"
- board text removed: "HDMI1"
- board text removed: "Raspberry Pi Compute Module 4 IO Board"
- board text removed: "Rev 5b"
- board text removed: "USB"
